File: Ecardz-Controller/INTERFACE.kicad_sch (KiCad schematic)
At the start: 0 parts

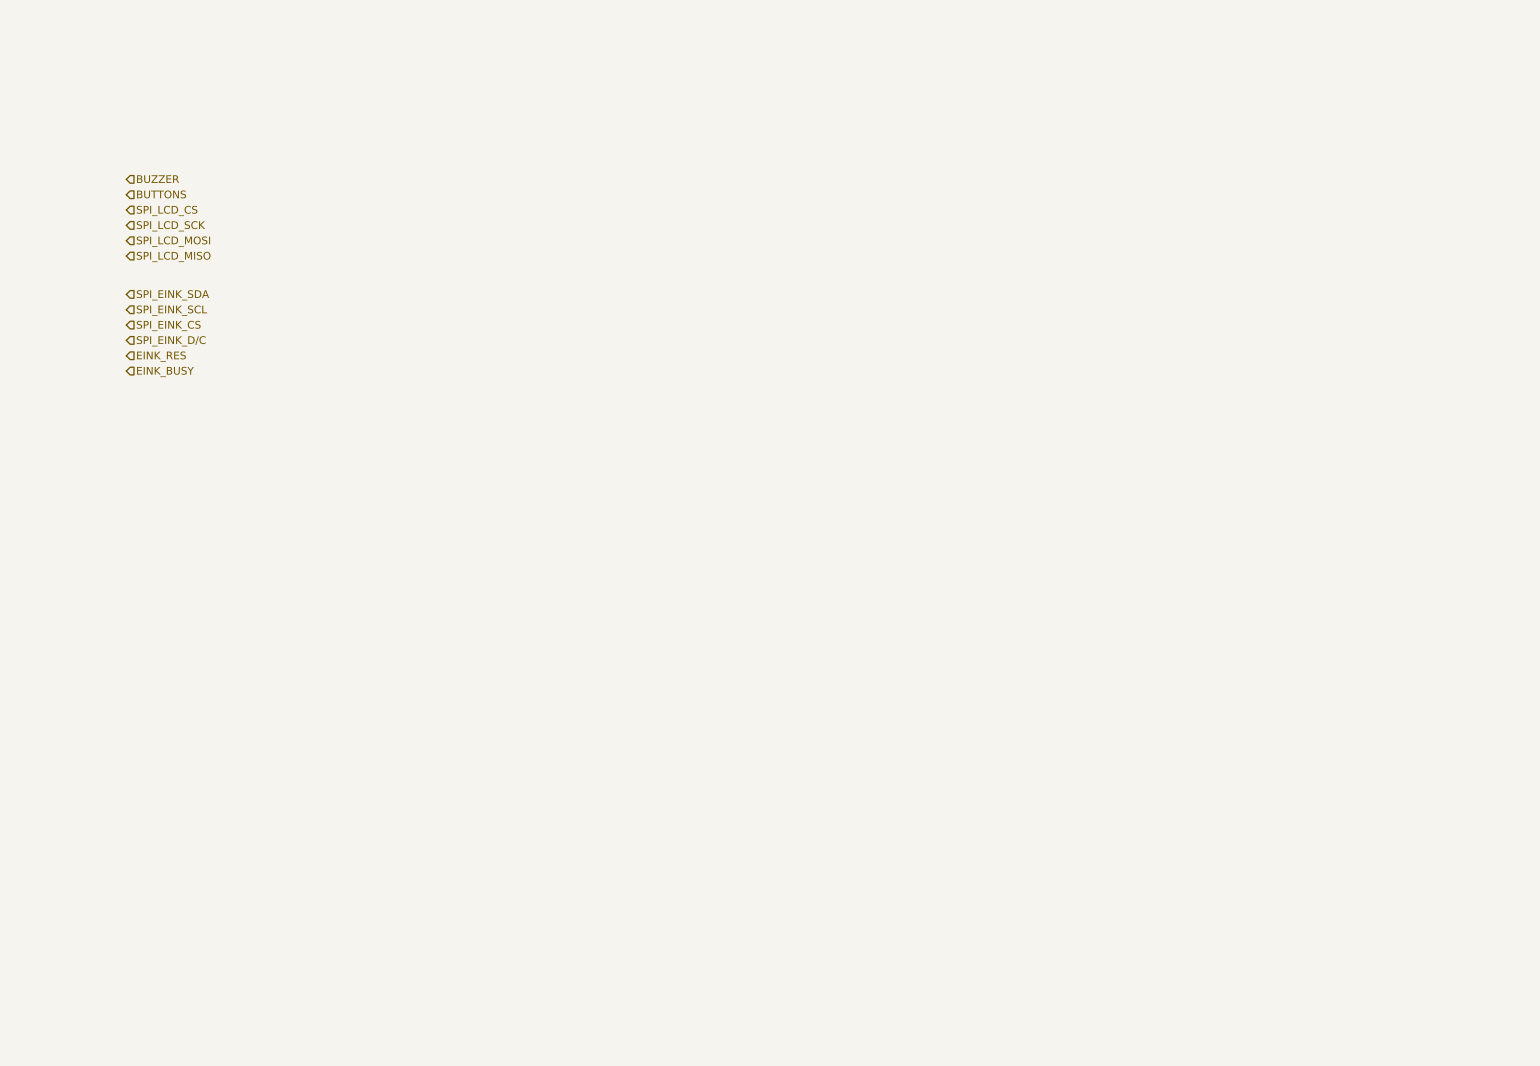
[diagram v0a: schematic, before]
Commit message: added eink and lcd pinouts
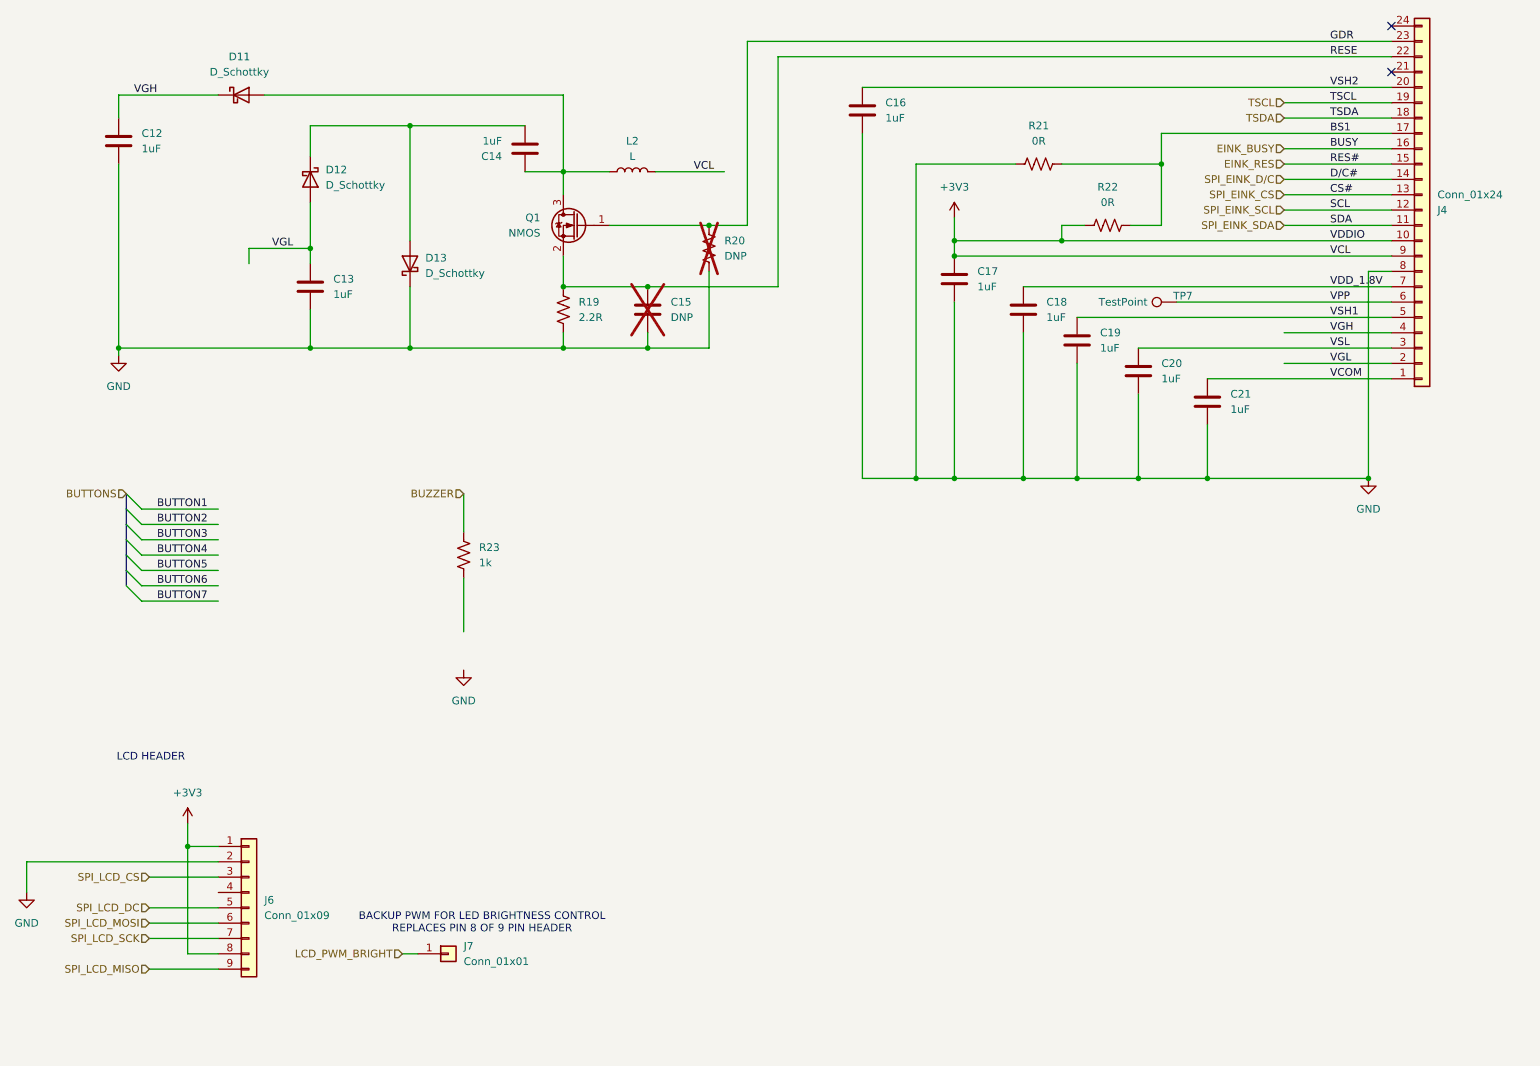
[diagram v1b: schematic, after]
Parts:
- added C12, C13, C14, C16, C17, C18, C19, C20, C21: 1uF, Capacitor_SMD:C_0603_1608Metric_Pad1.08x0.95mm_HandSolder, symbol Device:C
- added C15: DNP, Capacitor_SMD:C_0603_1608Metric_Pad1.08x0.95mm_HandSolder, symbol Device:C
- added D11, D12, D13: D_Schottky, Diode_SMD:D_SOD-123, symbol Device:D_Schottky
- added J4: Conn_01x24, Connector_FFC-FPC:TE_2-1734839-4_1x24-1MP_P0.5mm_Horizontal, symbol Connector_Generic:Conn_01x24
- added J6: Conn_01x09, symbol Connector_Generic:Conn_01x09
- added J7: Conn_01x01, symbol Connector_Generic:Conn_01x01
- added L2: L, parts-lib:CDRH5D18, symbol Device:L
- added Q1: NMOS, Package_TO_SOT_SMD:SOT-23, symbol Device:Q_NMOS_Depletion_GSD
- added R19: 2.2R, Resistor_SMD:R_0603_1608Metric_Pad0.98x0.95mm_HandSolder, symbol Device:R_US
- added R20: DNP, Resistor_SMD:R_0603_1608Metric_Pad0.98x0.95mm_HandSolder, symbol Device:R_US
- added R21, R22: 0R, Resistor_SMD:R_0603_1608Metric_Pad0.98x0.95mm_HandSolder, symbol Device:R_US
- added R23: 1k, Resistor_SMD:R_0603_1608Metric_Pad0.98x0.95mm_HandSolder, symbol Device:R_US
- added TP7: TestPoint, TestPoint:TestPoint_Pad_1.0x1.0mm, symbol Connector:TestPoint
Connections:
- net BUZZER: now also R23.1
- net EINK_BUSY: now also J4.16 (Pin_16)
- net EINK_RES: now also J4.15 (Pin_15)
- net SPI_EINK_CS: now also J4.13 (Pin_13)
- net SPI_EINK_D/C: now also J4.14 (Pin_14)
- net SPI_EINK_SCL: now also J4.12 (Pin_12)
- net SPI_EINK_SDA: now also J4.11 (Pin_11)
- net SPI_LCD_CS: now also J6.3 (Pin_3)
- net SPI_LCD_MISO: now also J6.9 (Pin_9)
- net SPI_LCD_MOSI: now also J6.6 (Pin_6)
- net SPI_LCD_SCK: now also J6.7 (Pin_7)
- new net: C14.1, D11.2 (A), L2.1, Q1.3 (D)
- new net: C14.2, D12.1 (K), D13.2 (A)
- new net +3V3: C17.1, J4.10 (Pin_10), J4.9 (Pin_9), J6.1 (Pin_1), J6.8 (Pin_8), L2.2, R22.1
- new net BS1: J4.17 (Pin_17), R21.2, R22.2
- new net GDR: J4.23 (Pin_23), Q1.1 (G), R20.1
- new net GND: C12.2, C13.2, C15.2, C16.2, C17.2, C18.2, C19.2, C20.2, C21.2, D13.1 (K), J4.8 (Pin_8), J6.2 (Pin_2), R19.2, R20.2, R21.1
- new net LCD_PWM_BRIGHT: J7.1 (Pin_1)
- new net RESE: C15.1, J4.22 (Pin_22), Q1.2 (S), R19.1
- new net SPI_LCD_DC: J6.5 (Pin_5)
- new net TSCL: J4.19 (Pin_19)
- new net TSDA: J4.18 (Pin_18)
- new net VCOM: C21.1, J4.1 (Pin_1)
- new net VDD_1.8V: C18.1, J4.7 (Pin_7)
- new net VGH: C12.1, D11.1 (K), J4.4 (Pin_4)
- new net VGL: C13.1, D12.2 (A), J4.2 (Pin_2)
- new net VPP: J4.6 (Pin_6), TP7.1
- new net VSH1: C19.1, J4.5 (Pin_5)
- new net VSH2: C16.1, J4.20 (Pin_20)
- new net VSL: C20.1, J4.3 (Pin_3)
- no-connect marks 0 -> 2
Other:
- note added: "BACKUP PWM FOR LED BRIGHTNESS CONTROL REPLACES PIN 8 OF 9 PIN HEADER"
- note added: "LCD HEADER"

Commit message: finished buzzer and button connections
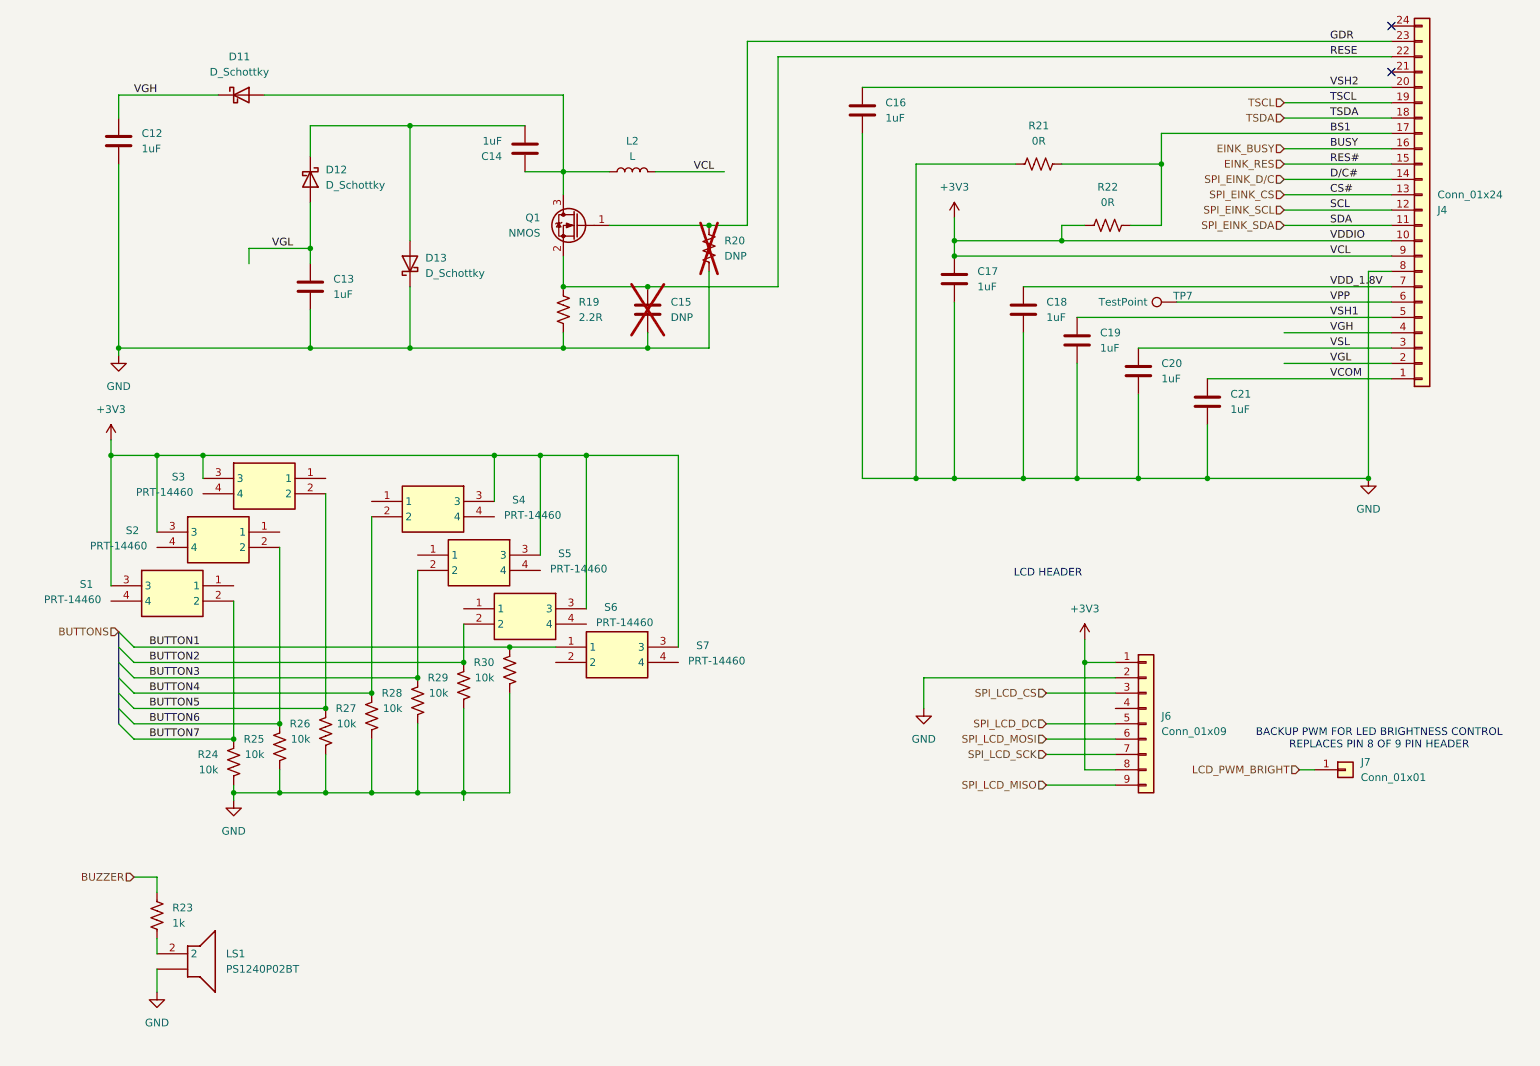
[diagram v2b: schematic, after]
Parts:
- added LS1: PS1240P02BT, PS1240P02BT, symbol SamacSys_Parts:PS1240P02BT
- added R24, R25, R26, R27, R28, R29, R30: 10k, Resistor_SMD:R_0603_1608Metric_Pad0.98x0.95mm_HandSolder, symbol Device:R_US
- added S1, S2, S3, S4, S5, S6, S7: PRT-14460, PRT14460, symbol SamacSys_Parts:PRT-14460
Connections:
- net +3V3: now also S1.3, S2.3, S3.3, S4.3, S5.3, S6.3, S7.3
- net BUTTON1: now also R30.1, S7.1
- net BUTTON2: now also R29.1, S6.2
- net BUTTON3: now also R28.1, S5.2
- net BUTTON4: now also R27.1, S4.2
- net BUTTON5: now also R26.1, S3.2
- net BUTTON6: now also R25.1, S2.2
- net BUTTON7: now also R24.1, S1.2
- net GND: now also LS1., R24.2, R25.2, R26.2, R27.2, R28.2, R29.2, R30.2
- net at R23.2: now also LS1.2
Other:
- moved on the sheet: J6, J7, R23

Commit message: fixed FPC connector
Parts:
- J4: Digikey Part Number A101358TR-ND -> (none); MANUFACTURER PART NUMBER 4-1734839-5 -> 10051922-2410ELF; Part Number (none) -> 10051922-2410ELF
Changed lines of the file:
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@@
 			)
 		)
-		(property "Datasheet" "https://www.mouser.ca/datasheet/2/418/7/ENG_CD_1734839_C_C_1734839-2017397.pdf"
+		(property "Datasheet" "https://www.digikey.ca/en/products/detail/amphenol-cs-fci/10051922-2410ELF/1001555"
 			(at 248.92 54.61 0)
 			(effects
@@
 			)
 		)
-		(property "MANUFACTURER PART NUMBER" "4-1734839-5"
+		(property "MANUFACTURER PART NUMBER" "10051922-2410ELF"
 			(at 248.92 54.61 0)
 			(effects
@@
 			)
 		)
-		(property "Digikey Part Number" "A101358TR-ND"
+		(property "Part Number" "10051922-2410ELF"
 			(at 248.92 54.61 0)
 			(effects

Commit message: initial work on controller layout
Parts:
- R29: renamed from R22; now not fitted
- renumbered C12 to C23, C13 to C24, C14 to C25, C15 to C26, C16 to C27, C17 to C28, C18 to C29, C19 to C30, C20 to C31, C21 to C32, D12 to D10, D13 to D11, D11 to D9, J6 to J4, J7 to J5, J4 to J6, L2 to L1, R23 to R18, R24 to R19, R25 to R20, R26 to R21, R27 to R22, R28 to R23, R29 to R24, R30 to R25, R19 to R26, R20 to R27, R21 to R28, TP7 to TP3

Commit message: did bulk of controller layout apart from the antenna, added some NCs and other minor clean ups on schematic
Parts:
- J4: footprint (none) -> Connector_PinHeader_2.54mm:PinHeader_1x09_P2.54mm_Vertical
- J5: footprint (none) -> Connector_PinHeader_2.54mm:PinHeader_1x01_P2.54mm_Vertical
- LS1: footprint PS1240P02BT -> samacsys:PS1240P02BT
- S1, S2, S3, S4, S5, S6, S7: footprint PRT14460 -> samacsys:PRT14460
- TP3: footprint TestPoint:TestPoint_Pad_1.0x1.0mm -> TestPoint:TestPoint_Pad_D3.0mm
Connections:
- net BUTTON1: now also R19.1, S1.2; no longer R25.1, S7.1
- net BUTTON2: now also R20.1, S2.2; no longer R24.1, S6.2
- net BUTTON3: now also R21.1, S3.2; no longer R23.1, S5.2
- net BUTTON5: now also R23.1, S5.2; no longer R21.1, S3.2
- net BUTTON6: now also R24.1, S6.2; no longer R20.1, S2.2
- net BUTTON7: now also R25.1, S7.2; no longer R19.1, S1.2
- no-connect marks 2 -> 17

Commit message: controller updates
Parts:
- removed S7: PRT-14460, samacsys:PRT14460, symbol SamacSys_Parts:PRT-14460
- added J9: Conn_01x04, Connector_PinHeader_2.54mm:PinHeader_1x04_P2.54mm_Horizontal, symbol Connector_Generic:Conn_01x04
- added R12: 10k, Resistor_SMD:R_0603_1608Metric_Pad0.98x0.95mm_HandSolder, symbol Device:R_US
- C23, C24, C25, C27, C28, C29, C30, C31, C32: Part Number (none) -> CL10B105KP8NNNC
- D10, D11, D9: Part Number (none) -> BAT54T1G
- J4: Part Number (none) -> 61300911121
- J5: Part Number (none) -> 61300111121
- L1: Part Number (none) -> CDRH5D18
- LS1: Part Number (none) -> PS1240P02BT
- Q1: Part Number (none) -> T2N7002AK,LM
- R27: renamed from R26; Part Number (none) -> CRCW06032R20FKEAC
- R29: renamed from R28; Part Number (none) -> RMCF0603ZT0R00
- R30: renamed from R29; Part Number (none) -> RMCF0603ZT0R00
- S1, S2, S3, S4, S5, S6: Part Number (none) -> PRT-14460
- renumbered R18 to R19, R19 to R20, R20 to R21, R21 to R22, R22 to R23, R23 to R24, R24 to R25, R25 to R26, R27 to R28
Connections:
- net +3V3: now also J9.1 (Pin_1)
- net BUTTON7: now also J9.2 (Pin_2)
- net GND: now also LS1.1, R12.2; no longer LS1.
- new net: J9.4 (Pin_4), R12.1
- new net PWR_INDICATOR: J9.3 (Pin_3)
- no-connect marks 17 -> 15
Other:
- note added: "Power indicator and switch"
- moved on the sheet: R26

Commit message: added current sense resistor and modified buzzer circuit
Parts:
- added Q2: TMBT3904,LM, TMBT3904LM, symbol SamacSys_Parts:TMBT3904,LM
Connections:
- net +3V3: now also LS1.2, R19.1
- net BUZZER: now also Q2.1 (B); no longer R19.1
- net GND: now also Q2.2 (E); no longer LS1.1
- net at R19.2: now also LS1.1, Q2.3 (C); no longer LS1.2
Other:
- moved on the sheet: LS1, R19

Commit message: redid MCU connections from IOC file from FW team
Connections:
- net SPI_EINK_SCL renamed SPI_EINK_SCK
- net SPI_EINK_SDA renamed SPI_EINK_MOSI
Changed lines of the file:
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@@
 		)
 	)
-	(hierarchical_label "SPI_EINK_SDA"
+	(hierarchical_label "SPI_EINK_MOSI"
 		(shape input)
 		(at 226.06 57.15 180)
@@
 		)
 	)
-	(hierarchical_label "SPI_EINK_SCL"
+	(hierarchical_label "SPI_EINK_SCK"
 		(shape input)
 		(at 226.06 54.61 180)
